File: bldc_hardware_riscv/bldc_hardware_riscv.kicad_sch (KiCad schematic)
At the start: 41 parts

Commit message: use hall current sensor (60A limit), use keystone terminal, support up to 120V input
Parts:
- added U: (no value), symbol Device:R
- added U: (no value), symbol Switch:SW_Push
- added U: (no value), symbol Device:LED
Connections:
- net 3.3V: now also U.2
- net GND: now also U.1 (K), U.2
- net NRST: now also U.1
- new net: U.1, U.2 (A)
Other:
- note added: "1.1.0"
- note added: "Push SW1 & SW2 to load ISP"
- note removed: "1.0.1"
- note removed: "Push & Power up to load ISP"
- moved on the sheet: U

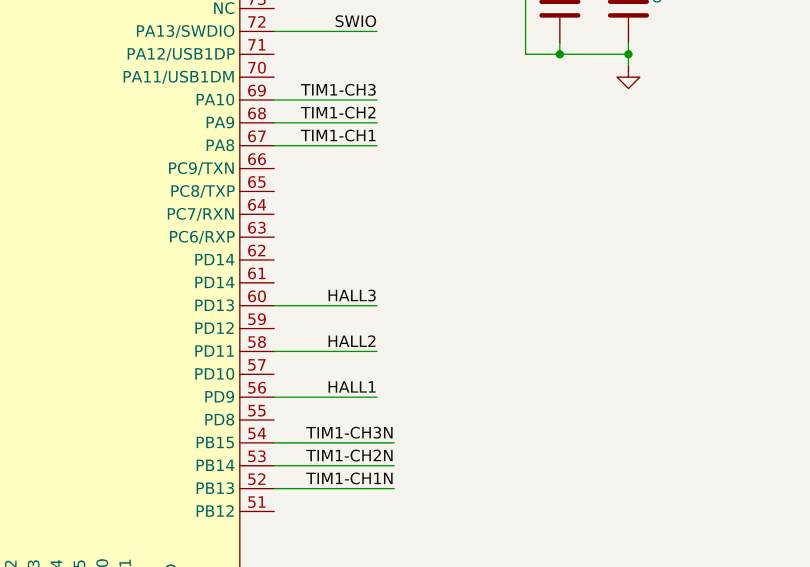
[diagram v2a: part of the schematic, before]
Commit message: Update WCH LOGO, fixed gbr clearance issue (around MCU range)
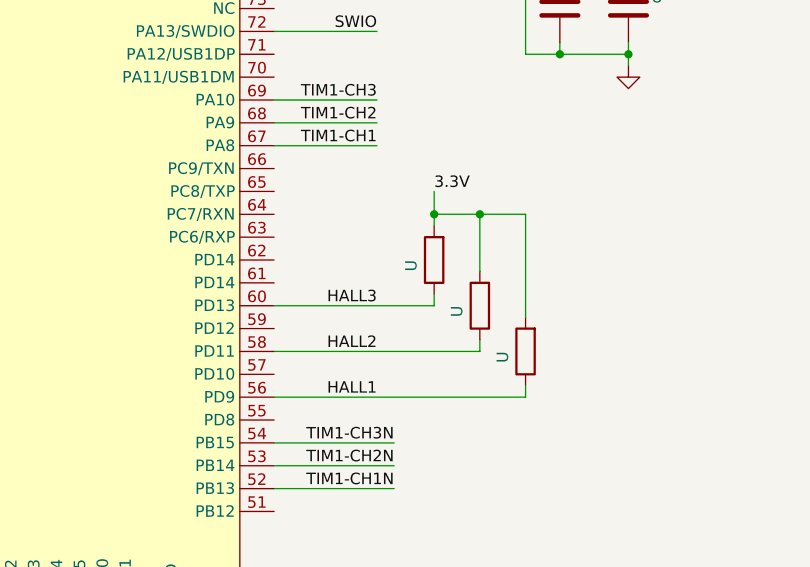
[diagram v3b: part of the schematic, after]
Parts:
- added U (x3): (no value), symbol Device:R
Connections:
- net 3.3V: now also U.2, U.2, U.2
- net HALL1: now also U.1
- net HALL2: now also U.1
- net HALL3: now also U.1
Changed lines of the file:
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@@
   (junction (at 21.59 43.18) (diameter 0) (color 0 0 0 0)
   )
+  (junction (at 176.53 86.36) (diameter 0) (color 0 0 0 0)
+  )
   (junction (at 185.42 68.58) (diameter 0) (color 0 0 0 0)
   )
+  (junction (at 171.45 86.36) (diameter 0) (color 0 0 0 0)
+  )
   (junction (at 257.81 123.19) (diameter 0) (color 0 0 0 0)
   )
@@
     (stroke (width 0) (type default))
   )
+  (wire (pts (xy 176.53 86.36) (xy 171.45 86.36))
+    (stroke (width 0) (type default))
+  )
+  (wire (pts (xy 176.53 92.71) (xy 176.53 86.36))
+    (stroke (width 0) (type default))
+  )
   (wire (pts (xy 210.82 147.32) (xy 215.9 147.32))
     (stroke (width 0) (type default))
@@
     (stroke (width 0) (type default))
   )
+  (wire (pts (xy 181.61 97.79) (xy 181.61 86.36))
+    (stroke (width 0) (type default))
+  )
   (wire (pts (xy 96.52 133.35) (xy 96.52 142.24))
     (stroke (width 0) (type default))
@@
     (stroke (width 0) (type default))
   )
+  (wire (pts (xy 176.53 100.33) (xy 176.53 101.6))
+    (stroke (width 0) (type default))
+  )
   (wire (pts (xy 232.41 158.75) (xy 232.41 160.02))
     (stroke (width 0) (type default))
@@
     (stroke (width 0) (type default))
   )
+  (wire (pts (xy 171.45 95.25) (xy 171.45 96.52))
+    (stroke (width 0) (type default))
+  )
   (wire (pts (xy 115.57 21.59) (xy 119.38 21.59))
     (stroke (width 0) (type default))
   )
-  (wire (pts (xy 153.67 101.6) (xy 165.1 101.6))
+  (wire (pts (xy 153.67 101.6) (xy 176.53 101.6))
     (stroke (width 0) (type default))
   )
@@
     (stroke (width 0) (type default))
   )
+  (wire (pts (xy 181.61 86.36) (xy 176.53 86.36))
+    (stroke (width 0) (type default))
+  )
   (wire (pts (xy 21.59 41.91) (xy 21.59 43.18))
     (stroke (width 0) (type default))
@@
     (stroke (width 0) (type default))
   )
+  (wire (pts (xy 171.45 83.82) (xy 171.45 86.36))
+    (stroke (width 0) (type default))
+  )
   (wire (pts (xy 267.97 135.89) (xy 275.59 135.89))
     (stroke (width 0) (type default))
@@
     (stroke (width 0) (type default))
   )
-  (wire (pts (xy 153.67 96.52) (xy 165.1 96.52))
+  (wire (pts (xy 153.67 96.52) (xy 171.45 96.52))
     (stroke (width 0) (type default))
   )
@@
     (stroke (width 0) (type default))
   )
+  (wire (pts (xy 171.45 86.36) (xy 171.45 87.63))
+    (stroke (width 0) (type default))
+  )
   (wire (pts (xy 21.59 72.39) (xy 21.59 71.12))
     (stroke (width 0) (type default))
@@
     (stroke (width 0) (type default))
   )
+  (wire (pts (xy 181.61 105.41) (xy 181.61 106.68))
+    (stroke (width 0) (type default))
+  )
   (wire (pts (xy 278.13 105.41) (xy 273.05 105.41))
     (stroke (width 0) (type default))
@@
     (stroke (width 0) (type default))
   )
-  (wire (pts (xy 153.67 106.68) (xy 165.1 106.68))
+  (wire (pts (xy 153.67 106.68) (xy 181.61 106.68))
     (stroke (width 0) (type default))
   )
@@
   )
   (label "3.3V" (at 200.66 144.78 0) (fields_autoplaced)
+    (effects (font (size 1.27 1.27)) (justify left bottom))
+  )
+  (label "3.3V" (at 171.45 83.82 0) (fields_autoplaced)
     (effects (font (size 1.27 1.27)) (justify left bottom))
   )
@@
     (pin "1")
   )
+  (symbol (lib_id "Device:R") (at 181.61 101.6 180) (unit 1)
+    (in_bom yes) (on_board yes)
+    (default_instance (reference "U") (unit 1) (value "") (footprint ""))
+    (property "Reference" "U" (id 0) (at 179.07 102.8701 90)
+      (effects (font (size 1.27 1.27)) (justify right))
+    )
+    (property "Value" "" (id 1) (at 181.61 101.6 90)
+      (effects (font (size 1.27 1.27)))
+    )
+    (property "Footprint" "" (id 2) (at 183.388 101.6 90)
+      (effects (font (size 1.27 1.27)) hide)
+    )
+    (property "Datasheet" "~" (id 3) (at 181.61 101.6 0)
+      (effects (font (size 1.27 1.27)) hide)
+    )
+    (pin "1")
+    (pin "2")
+  )
   (symbol (lib_id "power:GND") (at 248.92 149.86 0) (unit 1)
     (in_bom yes) (on_board yes)
@@
     (pin "2")
   )
+  (symbol (lib_id "Device:R") (at 171.45 91.44 180) (unit 1)
+    (in_bom yes) (on_board yes)
+    (default_instance (reference "U") (unit 1) (value "") (footprint ""))
+    (property "Reference" "U" (id 0) (at 168.91 92.7101 90)
+      (effects (font (size 1.27 1.27)) (justify right))
+    )
+    (property "Value" "" (id 1) (at 171.45 91.44 90)
+      (effects (font (size 1.27 1.27)))
+    )
+    (property "Footprint" "" (id 2) (at 173.228 91.44 90)
+      (effects (font (size 1.27 1.27)) hide)
+    )
+    (property "Datasheet" "~" (id 3) (at 171.45 91.44 0)
+      (effects (font (size 1.27 1.27)) hide)
+    )
+    (pin "1")
+    (pin "2")
+  )
+  (symbol (lib_id "Device:R") (at 176.53 96.52 180) (unit 1)
+    (in_bom yes) (on_board yes)
+    (default_instance (reference "U") (unit 1) (value "") (footprint ""))
+    (property "Reference" "U" (id 0) (at 173.99 97.7901 90)
+      (effects (font (size 1.27 1.27)) (justify right))
+    )
+    (property "Value" "" (id 1) (at 176.53 96.52 90)
+      (effects (font (size 1.27 1.27)))
+    )
+    (property "Footprint" "" (id 2) (at 178.308 96.52 90)
+      (effects (font (size 1.27 1.27)) hide)
+    )
+    (property "Datasheet" "~" (id 3) (at 176.53 96.52 0)
+      (effects (font (size 1.27 1.27)) hide)
+    )
+    (pin "1")
+    (pin "2")
+  )
   (symbol (lib_id "Device:LED") (at 255.27 135.89 0) (unit 1)
     (in_bom yes) (on_board yes)
@@
       (reference "R17") (unit 1) (value "150K") (footprint "Resistor_SMD:R_0603_1608Metric")
     )
+    (path "/7a35f37b-d9a2-452e-84d4-c92ef633b56d"
+      (reference "R18") (unit 1) (value "2K2") (footprint "Resistor_SMD:R_0603_1608Metric")
+    )
+    (path "/7e83a1b6-3c46-4e86-b9be-afb868453515"
+      (reference "R19") (unit 1) (value "2K2") (footprint "Resistor_SMD:R_0603_1608Metric")
+    )
+    (path "/5b4128ea-f004-4922-80f4-9dfc5d235748"
+      (reference "R20") (unit 1) (value "2K2") (footprint "Resistor_SMD:R_0603_1608Metric")
+    )
     (path "/d07e27a0-6119-41cb-941d-798ad98c7227"
